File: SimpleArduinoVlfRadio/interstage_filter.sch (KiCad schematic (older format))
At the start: 3 parts

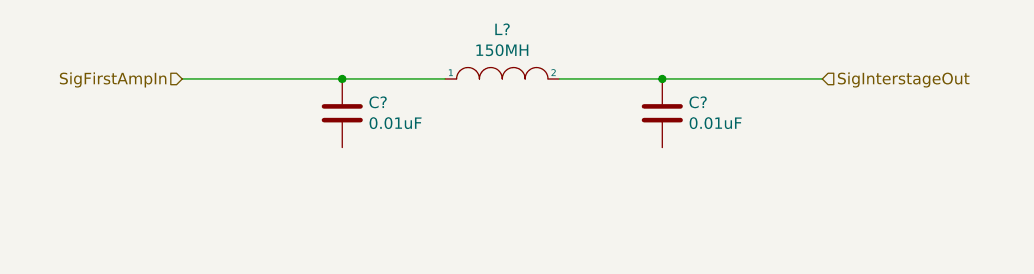
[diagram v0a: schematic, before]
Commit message: Add gnd connection to interstage filter
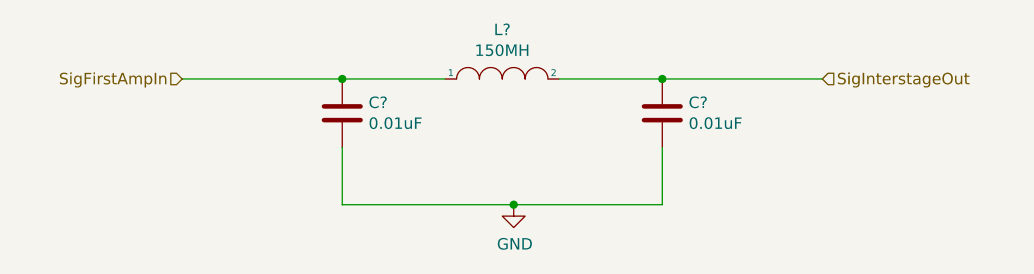
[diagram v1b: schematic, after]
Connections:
- net GND: now reaches C?.2
- net GND: now also C?.2
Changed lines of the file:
@@
 	6550 3500 7250 3500
 Connection ~ 6550 3500
+$Comp
+L power:GND #PWR?
+U 1 1 62C34CEC
+P 5900 4050
+F 0 "#PWR?" H 5900 3800 50  0001 C CNN
+F 1 "GND" H 5905 3877 50  0000 C CNN
+F 2 "" H 5900 4050 50  0001 C CNN
+F 3 "" H 5900 4050 50  0001 C CNN
+	1    5900 4050
+	1    0    0    -1
+$EndComp
+Wire Wire Line
+	6550 3800 6550 4050
+Wire Wire Line
+	6550 4050 5900 4050
+Wire Wire Line
+	5150 3800 5150 4050
+Wire Wire Line
+	5150 4050 5900 4050
+Connection ~ 5900 4050
 $EndSCHEMATC
